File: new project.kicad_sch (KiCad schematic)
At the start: 4 parts, among them J1 LED 0.170amps, J2 Tractive Battery

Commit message: FInished
Done
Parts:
- removed J1: LED 0.170amps, Connector_Molex:Molex_Micro-Fit_3.0_43650-0200_1x02_P3.00mm_Horizontal, symbol Connector:Conn_01x02_Pin
- removed J2: Tractive Battery, Connector_Molex:Molex_Micro-Fit_3.0_43650-0200_1x02_P3.00mm_Horizontal, symbol Connector:Conn_01x02_Pin
- removed R1: 18000, Resistor_THT:R_Axial_DIN0207_L6.3mm_D2.5mm_P15.24mm_Horizontal, symbol Device:R
- removed U1: ~, Package_TO_SOT_SMD:TO-252-2, symbol IXCP10M90S:IXCP10M90S
- added J3: Tractive Battery, Connector_Molex:Molex_Micro-Fit_3.0_43650-0200_1x02_P3.00mm_Horizontal, symbol Connector:Conn_01x02_Pin
- added J4: LED 0.170amps, Connector_Molex:Molex_Micro-Fit_3.0_43650-0200_1x02_P3.00mm_Horizontal, symbol Connector:Conn_01x02_Pin
- added R2: 18000, Resistor_THT:R_Axial_DIN0207_L6.3mm_D2.5mm_P15.24mm_Horizontal, symbol Device:R
- added U2: ~, Package_TO_SOT_SMD:TO-252-2, symbol IXCP10M90S:IXCP10M90S
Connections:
- net GND: now also J3.1 (Pin_1), R2.1, U2.1 (Gate)
- new net: R2.2, U2.3 (Cathode)
- new net: J3.2 (Pin_2), J4.1 (Pin_1)
- new net: J4.2 (Pin_2), U2.2 (Anode)
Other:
- note removed: "Sorry the wiring is probably awful and wrong first progject"
- note removed: "The led can take up to 0.170"

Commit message: Is it working
Working
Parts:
- added H1, H2: MountingHole, MountingHole:MountingHole_2.1mm, symbol Mechanical:MountingHole
- R2: footprint Resistor_THT:R_Axial_DIN0207_L6.3mm_D2.5mm_P15.24mm_Horizontal -> Resistor_THT:R_Axial_DIN0207_L6.3mm_D2.5mm_P10.16mm_Horizontal
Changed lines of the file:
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@@
+	)
+	(symbol
+		(lib_id "Mechanical:MountingHole")
+		(at 83.82 162.56 0)
+		(unit 1)
+		(exclude_from_sim no)
+		(in_bom no)
+		(on_board yes)
+		(dnp no)
+		(fields_autoplaced yes)
+		(property "Reference" "H2"
+			(at 86.36 161.2899 0)
+			(effects
+				(font
+					(size 1.27 1.27)
+				)
+				(justify left)
+			)
+		)
+		(property "Value" "MountingHole"
+			(at 86.36 163.8299 0)
+			(effects
+				(font
+					(size 1.27 1.27)
+				)
+				(justify left)
+			)
+		)
+		(property "Footprint" "MountingHole:MountingHole_2.1mm"
+			(at 83.82 162.56 0)
+			(effects
+				(font
+					(size 1.27 1.27)
+				)
+				(hide yes)
+			)
+		)
+		(property "Datasheet" "~"
+			(at 83.82 162.56 0)
+			(effects
+				(font
+					(size 1.27 1.27)
+				)
+				(hide yes)
+			)
+		)
+		(property "Description" "Mounting Hole without connection"
+			(at 83.82 162.56 0)
+			(effects
+				(font
+					(size 1.27 1.27)
+				)
+				(hide yes)
+			)
+		)
+		(instances
+			(project "new project"
+				(path "/077e92cf-3ae1-46e9-bd7c-3f2e84892e92"
+					(reference "H2")
+					(unit 1)
+				)
+			)
+		)
 	)
 	(symbol
@@
 			)
 		)
-		(property "Footprint" "Resistor_THT:R_Axial_DIN0207_L6.3mm_D2.5mm_P15.24mm_Horizontal"
+		(property "Footprint" "Resistor_THT:R_Axial_DIN0207_L6.3mm_D2.5mm_P10.16mm_Horizontal"
 			(at 50.038 160.02 90)
 			(effects
@@
 					(unit 1)
 				)
+			)
+		)
+	)
+	(symbol
+		(lib_id "Mechanical:MountingHole")
+		(at 76.2 152.4 0)
+		(unit 1)
+		(exclude_from_sim no)
+		(in_bom no)
+		(on_board yes)
+		(dnp no)
+		(fields_autoplaced yes)
+		(property "Reference" "H1"
+			(at 78.74 151.1299 0)
+			(effects
+				(font
+					(size 1.27 1.27)
+				)
+				(justify left)
+			)
+		)
+		(property "Value" "MountingHole"
+			(at 78.74 153.6699 0)
+			(effects
+				(font
+					(size 1.27 1.27)
+				)
+				(justify left)
+			)
+		)
+		(property "Footprint" "MountingHole:MountingHole_2.1mm"
+			(at 76.2 152.4 0)
+			(effects
+				(font
+					(size 1.27 1.27)
+				)
+				(hide yes)
+			)
+		)
+		(property "Datasheet" "~"
+			(at 76.2 152.4 0)
+			(effects
+				(font
+					(size 1.27 1.27)
+				)
+				(hide yes)
+			)
+		)
+		(property "Description" "Mounting Hole without connection"
+			(at 76.2 152.4 0)
+			(effects
+				(font
+					(size 1.27 1.27)
+				)
+				(hide yes)
+			)
+		)
+		(instances
+			(project ""
+				(path "/077e92cf-3ae1-46e9-bd7c-3f2e84892e92"
+					(reference "H1")
+					(unit 1)
+				)

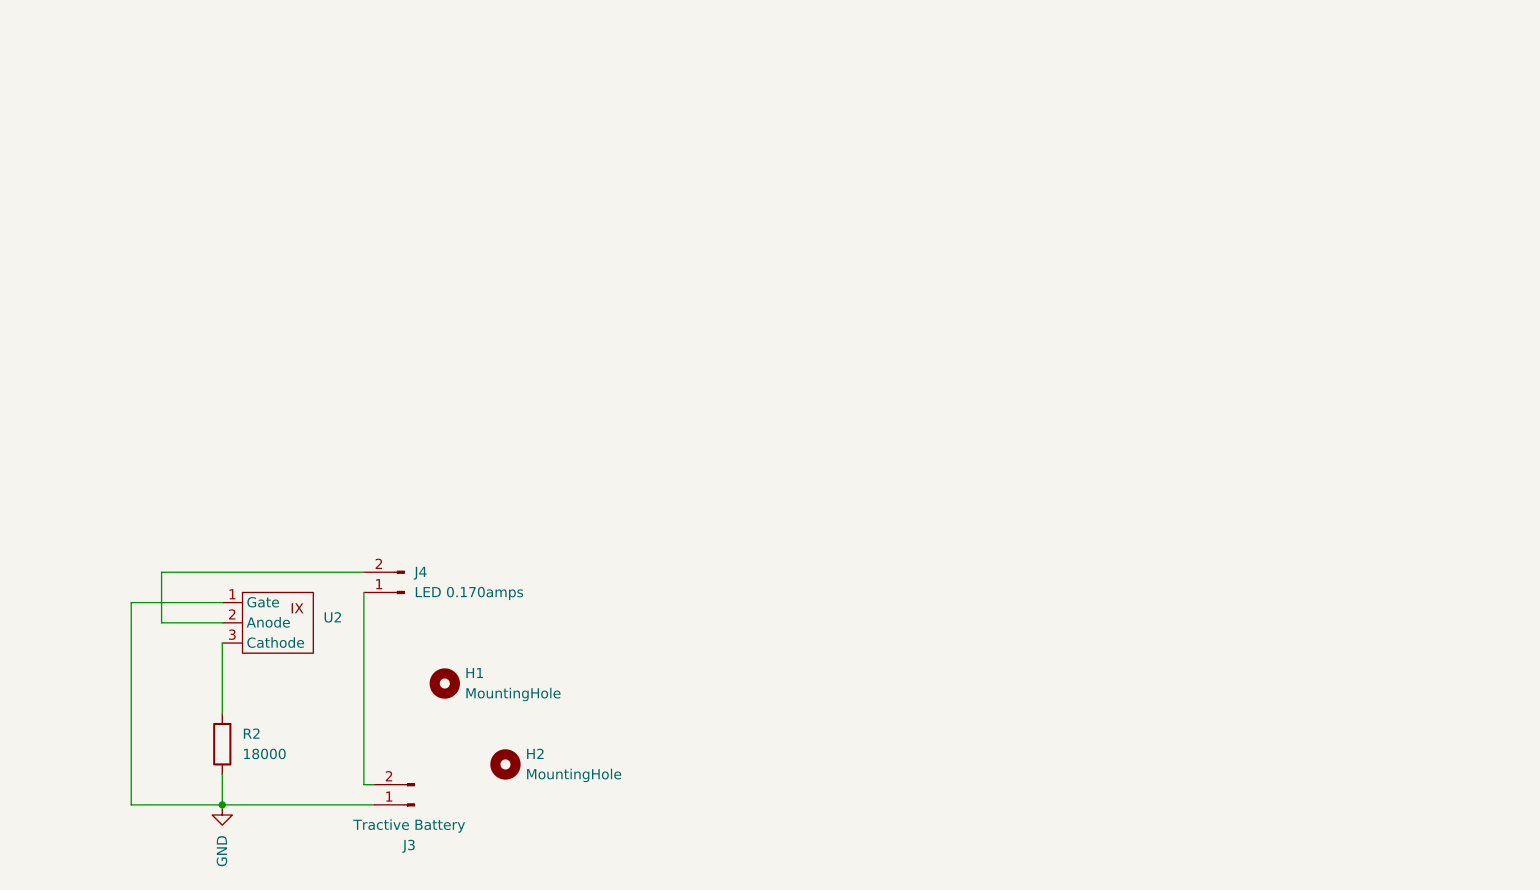
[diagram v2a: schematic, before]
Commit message: Updated Schematic
Based on new drawings
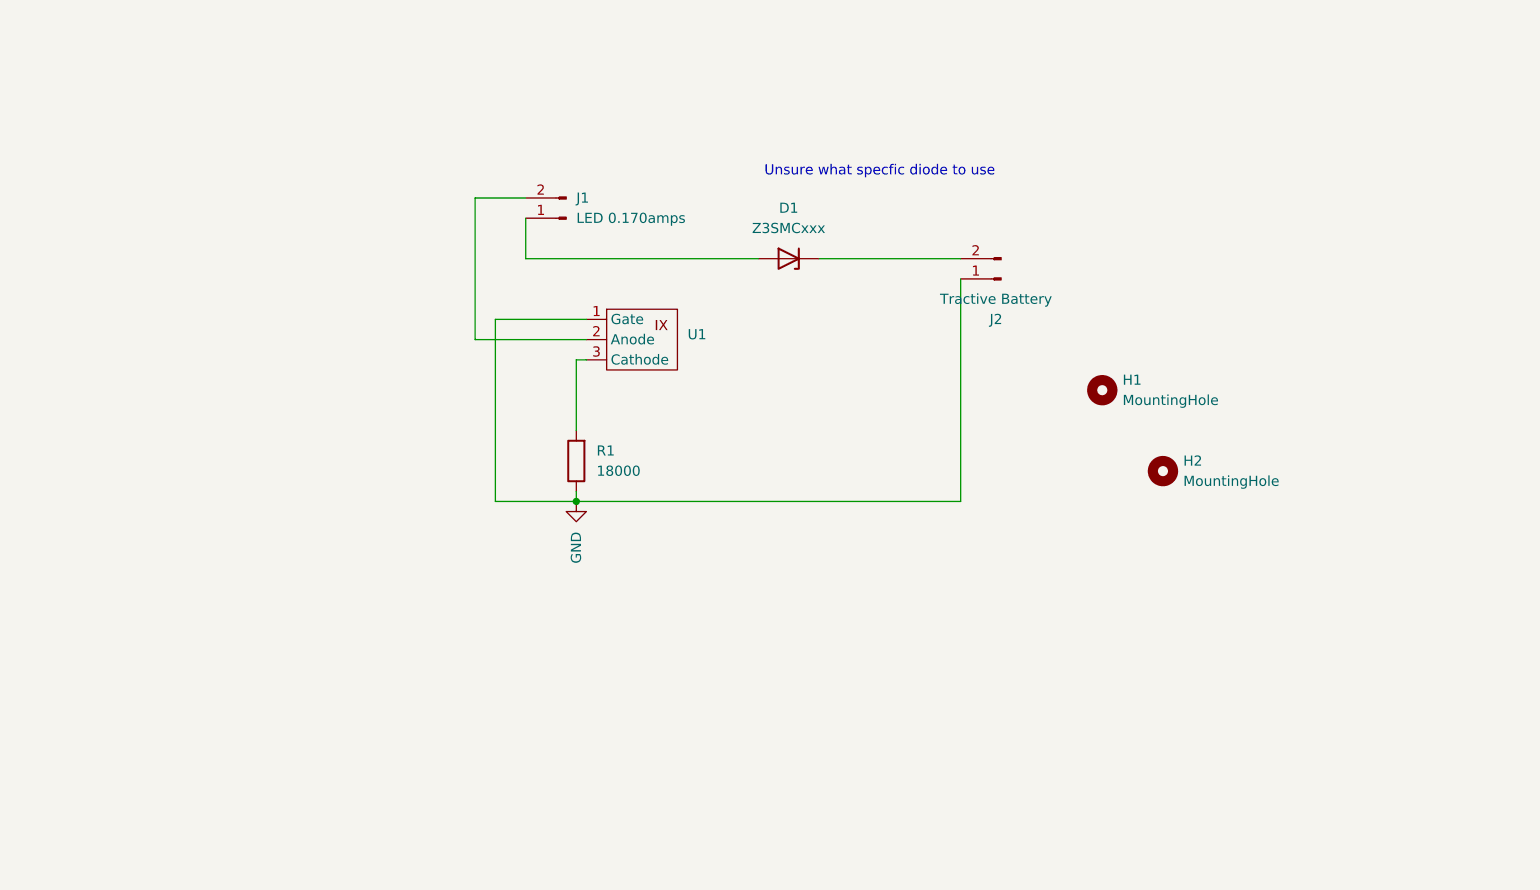
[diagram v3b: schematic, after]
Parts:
- removed J3: Tractive Battery, Connector_Molex:Molex_Micro-Fit_3.0_43650-0200_1x02_P3.00mm_Horizontal, symbol Connector:Conn_01x02_Pin
- removed J4: LED 0.170amps, Connector_Molex:Molex_Micro-Fit_3.0_43650-0200_1x02_P3.00mm_Horizontal, symbol Connector:Conn_01x02_Pin
- removed R2: 18000, Resistor_THT:R_Axial_DIN0207_L6.3mm_D2.5mm_P10.16mm_Horizontal, symbol Device:R
- removed U2: ~, Package_TO_SOT_SMD:TO-252-2, symbol IXCP10M90S:IXCP10M90S
- added D1: Z3SMCxxx, Diode_SMD:D_SMC, symbol Diode:Z3SMCxxx
- added J1: LED 0.170amps, Connector_Molex:Molex_Micro-Fit_3.0_43650-0200_1x02_P3.00mm_Horizontal, symbol Connector:Conn_01x02_Pin
- added J2: Tractive Battery, Connector_Molex:Molex_Micro-Fit_3.0_43650-0200_1x02_P3.00mm_Horizontal, symbol Connector:Conn_01x02_Pin
- added R1: 18000, Resistor_THT:R_Axial_DIN0207_L6.3mm_D2.5mm_P10.16mm_Horizontal, symbol Device:R
- added U1: ~, Package_TO_SOT_SMD:TO-252-2, symbol IXCP10M90S:IXCP10M90S
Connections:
- net GND: now also J2.1 (Pin_1), R1.1, U1.1 (Gate)
- new net: D1.1 (K), J2.2 (Pin_2)
- new net: D1.2 (A), J1.1 (Pin_1)
- new net: J1.2 (Pin_2), U1.2 (Anode)
- new net: R1.2, U1.3 (Cathode)
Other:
- note added: "Unsure what specfic diode to use"
- moved on the sheet: H1, H2

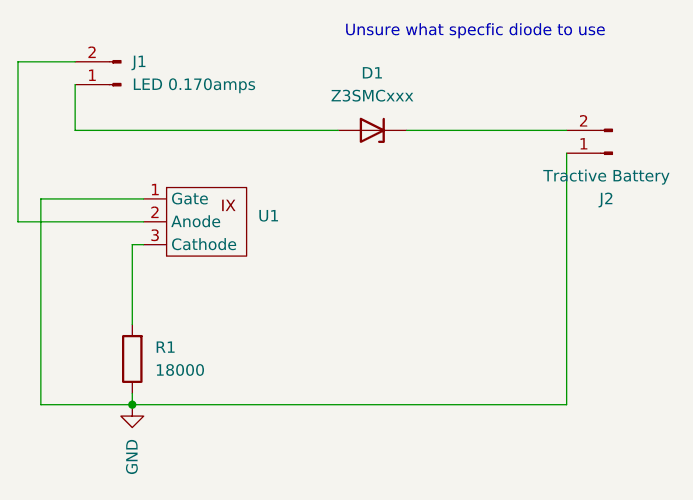
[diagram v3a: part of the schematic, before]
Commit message: Resistance Value Change
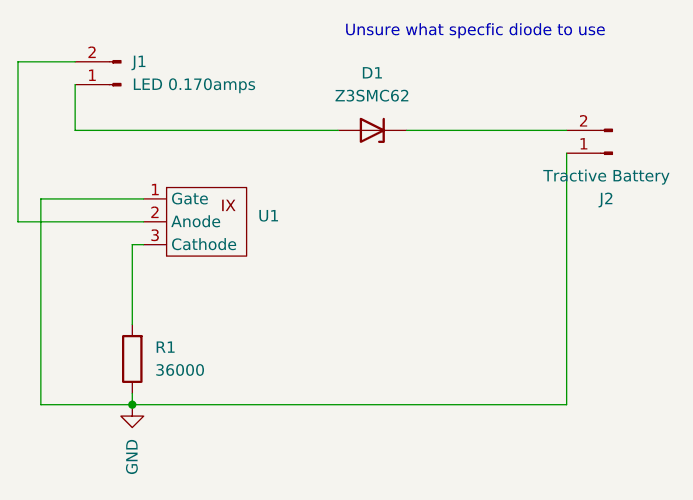
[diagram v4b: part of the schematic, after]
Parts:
- D1: value Z3SMCxxx -> Z3SMC62
- R1: value 18000 -> 36000
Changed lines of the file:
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@@
 			)
 		)
-		(property "Value" "Z3SMCxxx"
+		(property "Value" "Z3SMC62"
 			(at 119.38 95.25 0)
 			(effects
@@
 			)
 		)
-		(property "Value" "18000"
+		(property "Value" "36000"
 			(at 95.25 125.7299 0)
 			(effects

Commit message: G
sdafasddfsaf
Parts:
- removed U1: ~, Package_TO_SOT_SMD:TO-252-2, symbol IXCP10M90S:IXCP10M90S
- added C?: C, symbol Device:C
- added D?: D_Zener, symbol Device:D_Zener
- added Q?: Q_NPN_BCE, symbol Transistor_BJT:Q_NPN_BCE
- added Q?: Q_PNP_BCE, symbol Transistor_BJT:Q_PNP_BCE
- added R? (x2): R, symbol Device:R
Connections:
- new net: C?.1, Q?.1 (B), Q?.2 (C), R?.2
- new net: C?.2, Q?.3 (E), R?.2
- new net: Q?.1 (B), Q?.3 (E), R?.1
- new net: D?.2 (A), R?.1

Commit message: w
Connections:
- net GND: now also C?.2, Q?.3 (E), R?.2; no longer J2.1 (Pin_1), R1.1
- net at Q?.2 (C): now also J1.2 (Pin_2)
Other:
- moved on the sheet: C?, D?, J1, Q?, R1, R?

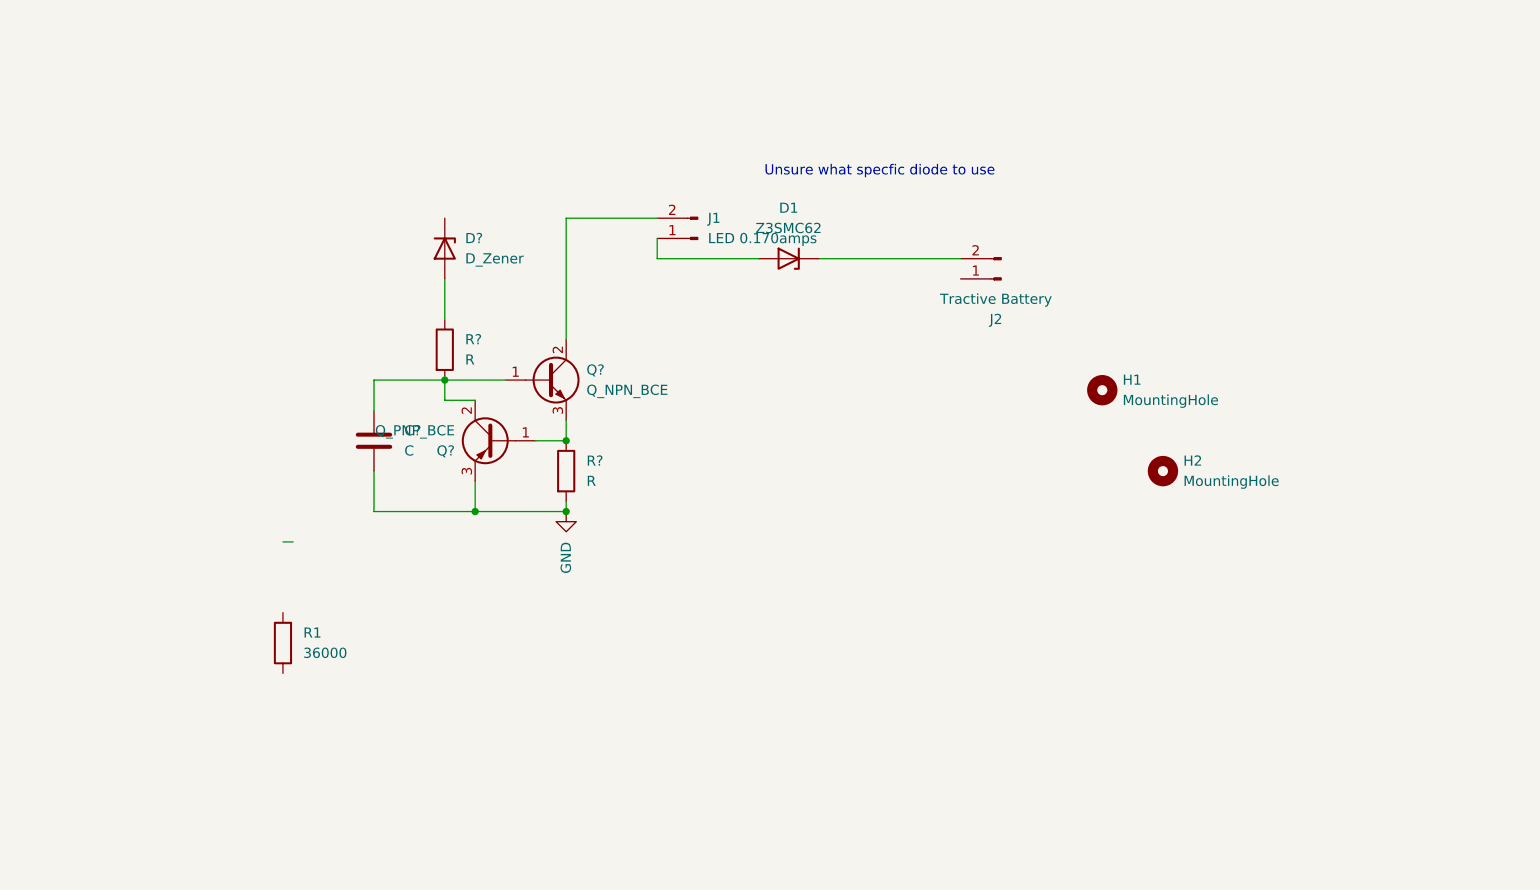
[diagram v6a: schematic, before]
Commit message: finished HVIL
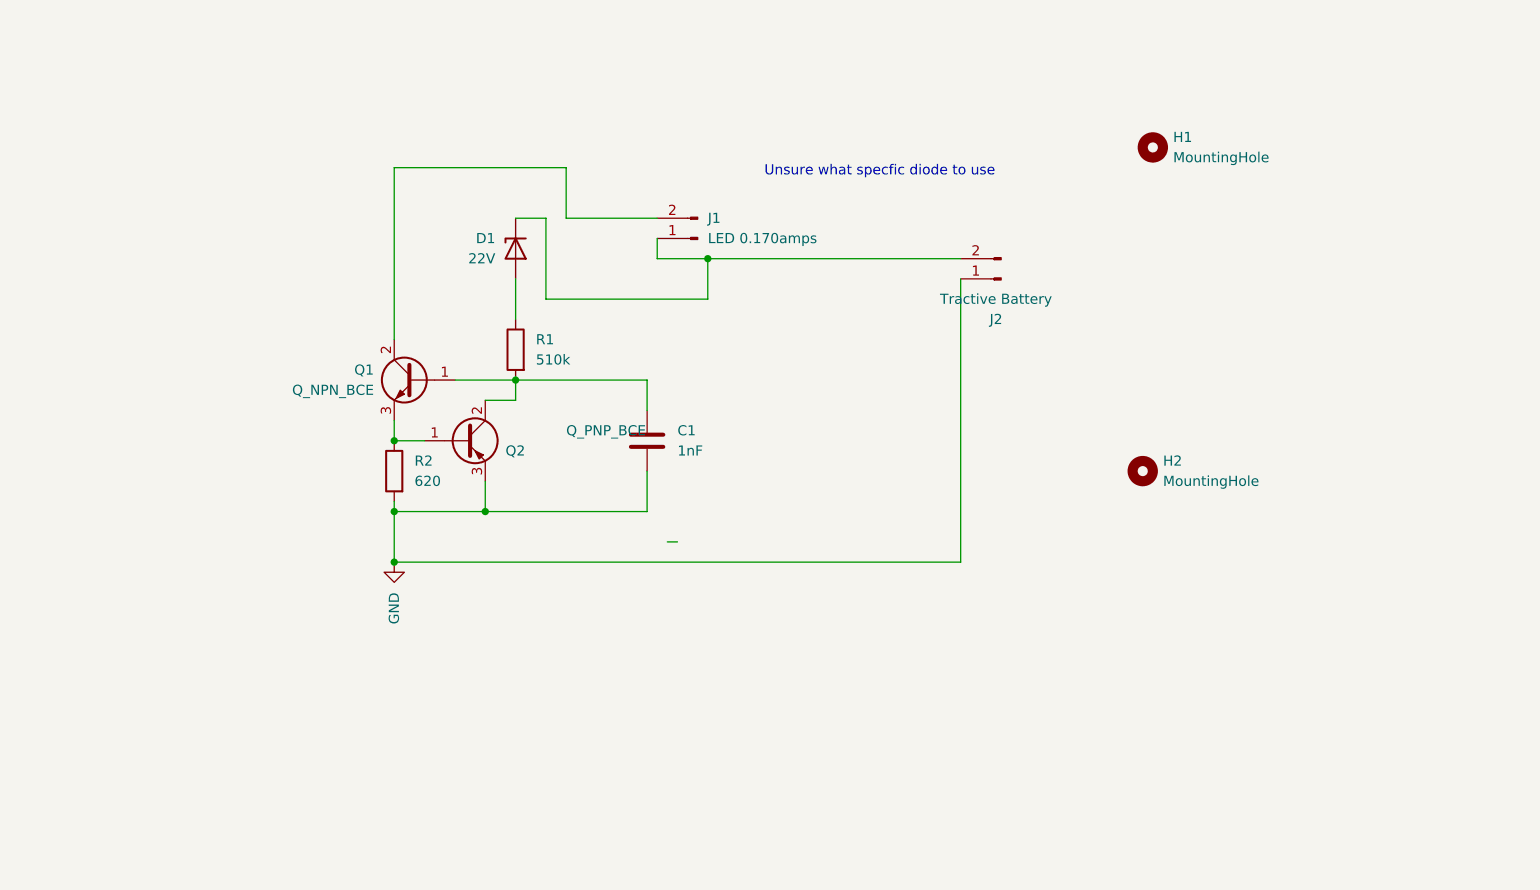
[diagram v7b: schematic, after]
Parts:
- removed D1: Z3SMC62, Diode_SMD:D_SMC, symbol Diode:Z3SMCxxx
- removed R1: 36000, Resistor_THT:R_Axial_DIN0207_L6.3mm_D2.5mm_P10.16mm_Horizontal, symbol Device:R
- C1: renamed from C?; value C -> 1nF; footprint (none) -> Capacitor_SMD:C_0603_1608Metric
- D1: renamed from D?; value D_Zener -> 22V; footprint (none) -> Diode_THT:D_DO-41_SOD81_P10.16mm_Horizontal
- Q1, Q2: renamed from Q?; footprint (none) -> Package_TO_SOT_SMD:SOT-223-3_TabPin2
- R1: renamed from R?; value R -> 510k; footprint (none) -> Resistor_SMD:R_2512_6332Metric
- R2: renamed from R?; value R -> 620; footprint (none) -> Resistor_SMD:R_2512_6332Metric
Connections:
- net GND: now also J2.1 (Pin_1)
- net at J2.2 (Pin_2): now also D1.1 (K), J1.1 (Pin_1)
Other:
- moved on the sheet: C1, D1, H1, H2, Q1, Q2, R1, R2
